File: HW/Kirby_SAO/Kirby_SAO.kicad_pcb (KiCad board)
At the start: 2 copper layers, 45.9 x 43.9 mm, 20 parts, among them X1 Badgelife_sao_connector_v169b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

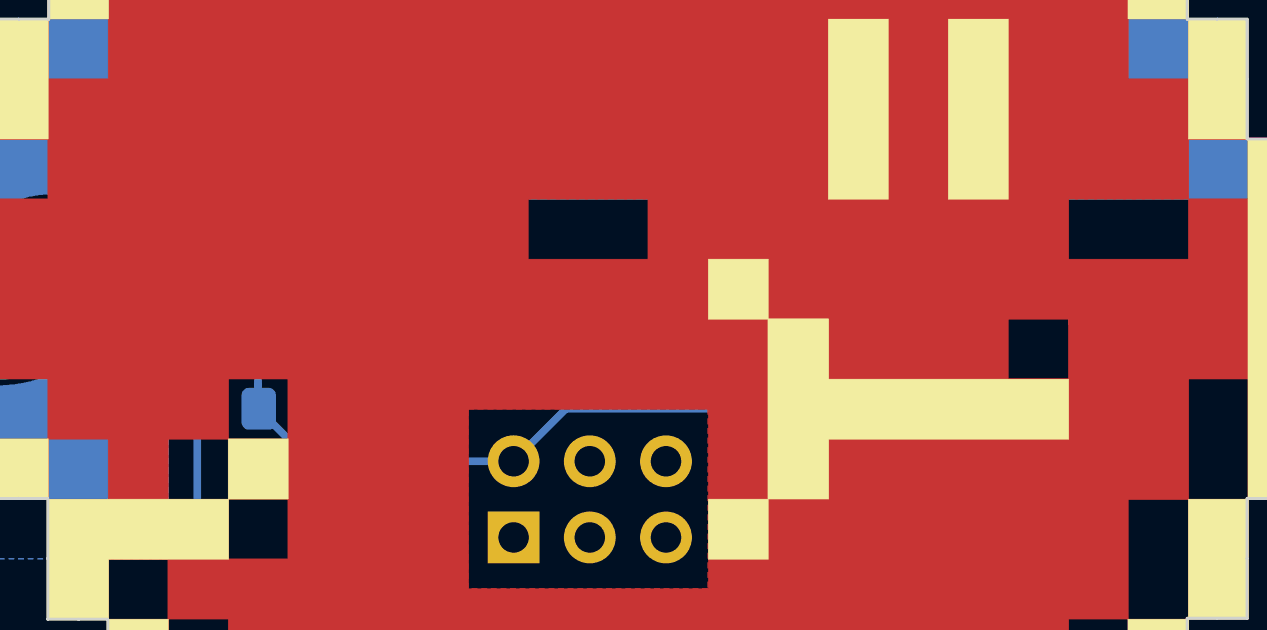
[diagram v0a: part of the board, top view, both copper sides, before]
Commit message: Finish B.Silk. Updated PCB with new silk and resistor layout
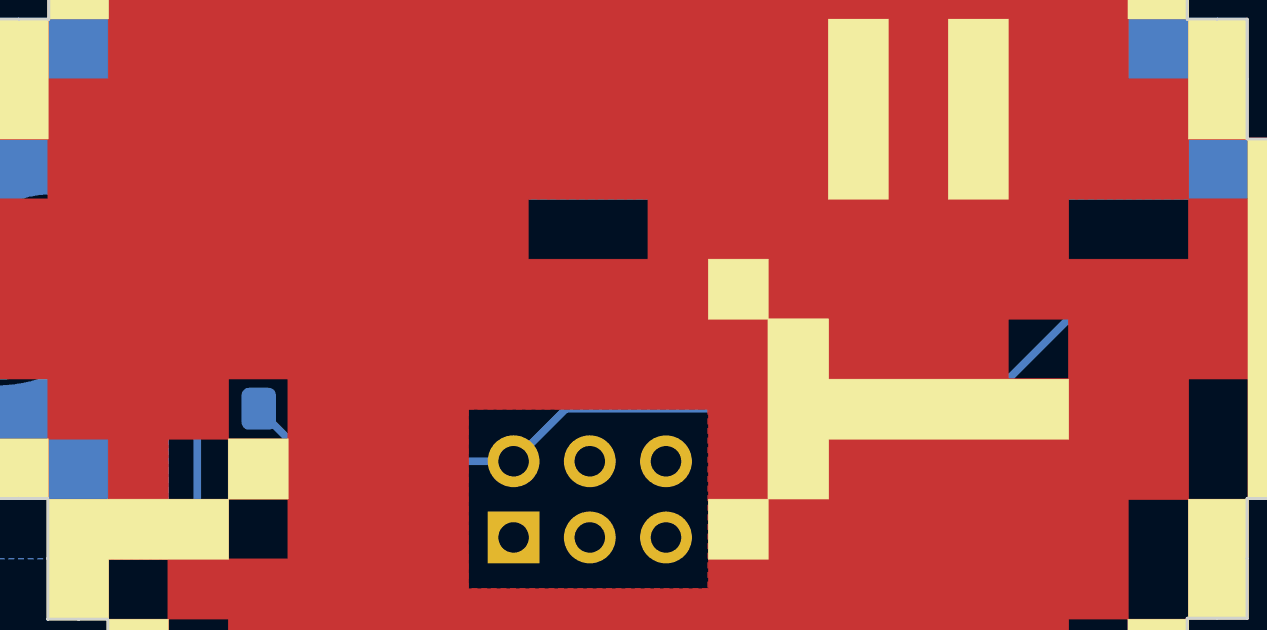
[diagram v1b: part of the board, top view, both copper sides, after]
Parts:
- removed the R1 at (87.0, 98.0)
- removed R3: 100R, Resistor_SMD:R_0805_2012Metric_Pad1.15x1.40mm_HandSolder
- added G*** (x2): LOGO, Kirby_SAO:B.Silk_g4152, F.Cu at (100.0, 100.0)
- R1: renamed from R2; value 100R -> 50R
- R2: renamed from R4; value 100R -> 50R
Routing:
- net VCC: track 33.3 -> 23.5 mm
- net Net-(D1-Pad2): track 62.4 -> 57.2 mm
- net Net-(D10-Pad2): track 48.8 -> 44.4 mm

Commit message: idk
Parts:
- removed the G*** at (100.0, 100.0)
